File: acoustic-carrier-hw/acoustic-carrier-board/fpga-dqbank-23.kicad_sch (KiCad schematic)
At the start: 11 parts, among them IC1 ECP5-BGA256

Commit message: [carrier] finished for production (next) reroute the LPDDR3, with appropriate CMD-CTRL bus delays, and change banks for command-control
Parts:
- IC1: Manufacturer Lattice -> (none)

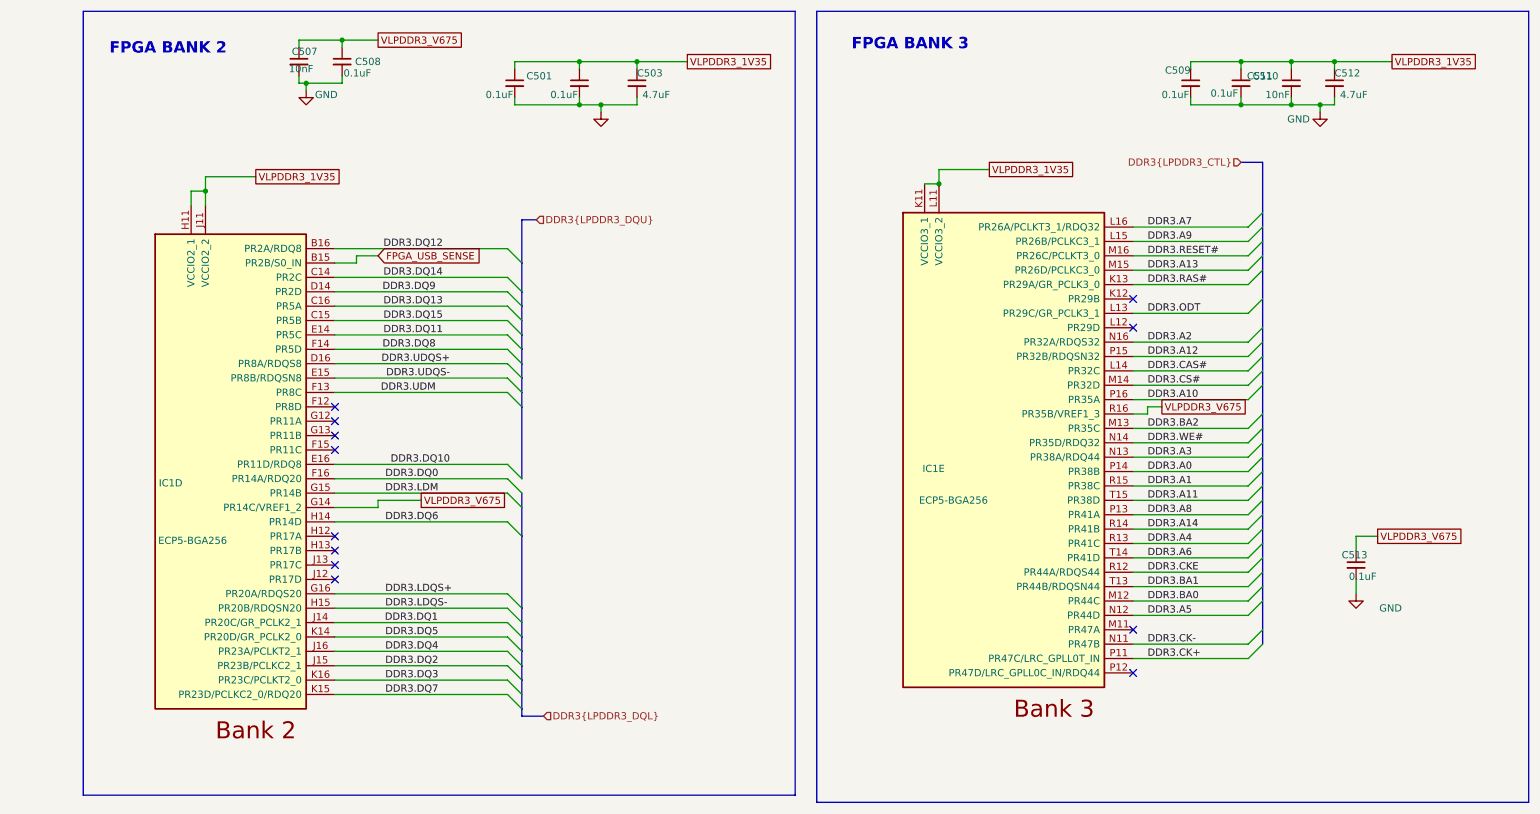
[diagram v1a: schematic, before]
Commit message: [carrier] Finished routing, layed out lpddr3 capacitors (next) route power on plane
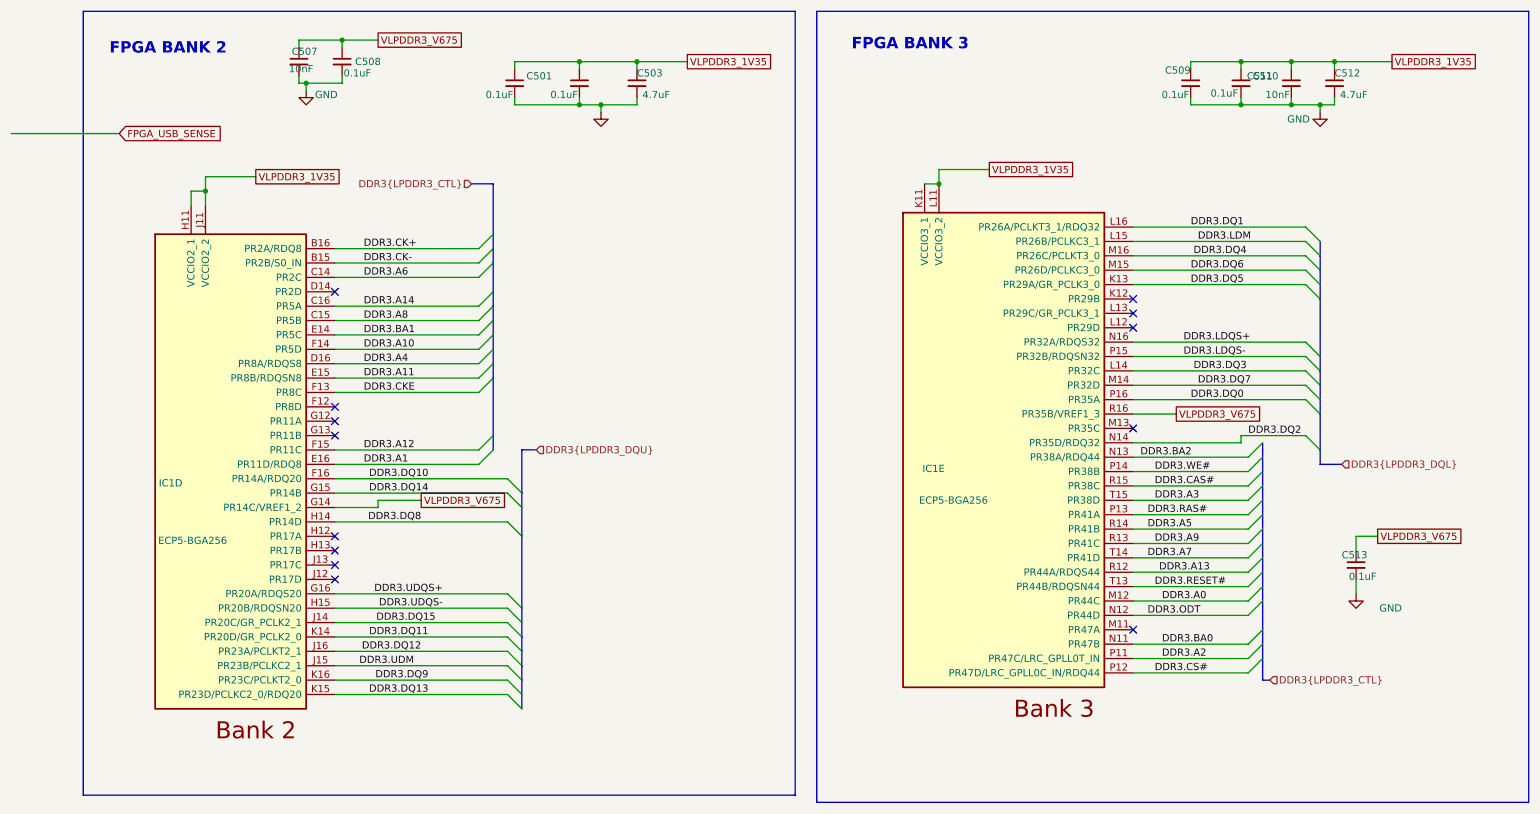
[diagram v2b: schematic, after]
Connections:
- net DDR3.A0: now also IC1.M12 (PR44C); no longer IC1.P14 (PR38B)
- net DDR3.A1: now also IC1.E16 (PR11D/RDQ8); no longer IC1.R15 (PR38C)
- net DDR3.A10: now also IC1.F14 (PR5D); no longer IC1.P16 (PR35A)
- net DDR3.A11: now also IC1.E15 (PR8B/RDQSN8); no longer IC1.T15 (PR38D)
- net DDR3.A12: now also IC1.F15 (PR11C); no longer IC1.P15 (PR32B/RDQSN32)
- net DDR3.A13: now also IC1.R12 (PR44A/RDQS44); no longer IC1.M15 (PR26D/PCLKC3_0)
- net DDR3.A14: now also IC1.C16 (PR5A); no longer IC1.R14 (PR41B)
- net DDR3.A2: now also IC1.P11 (PR47C/LRC_GPLL0T_IN); no longer IC1.N16 (PR32A/RDQS32)
- net DDR3.A3: now also IC1.T15 (PR38D); no longer IC1.N13 (PR38A/RDQ44)
- net DDR3.A4: now also IC1.D16 (PR8A/RDQS8); no longer IC1.R13 (PR41C)
- net DDR3.A5: now also IC1.R14 (PR41B); no longer IC1.N12 (PR44D)
- net DDR3.A6: now also IC1.C14 (PR2C); no longer IC1.T14 (PR41D)
- net DDR3.A7: now also IC1.T14 (PR41D); no longer IC1.L16 (PR26A/PCLKT3_1/RDQ32)
- net DDR3.A8: now also IC1.C15 (PR5B); no longer IC1.P13 (PR41A)
- net DDR3.A9: now also IC1.R13 (PR41C); no longer IC1.L15 (PR26B/PCLKC3_1)
- net DDR3.BA0: now also IC1.N11 (PR47B); no longer IC1.M12 (PR44C)
- net DDR3.BA1: now also IC1.E14 (PR5C); no longer IC1.T13 (PR44B/RDQSN44)
- net DDR3.BA2: now also IC1.N13 (PR38A/RDQ44); no longer IC1.M13 (PR35C)
- net DDR3.CAS#: now also IC1.R15 (PR38C); no longer IC1.L14 (PR32C)
- net DDR3.CK+: now also IC1.B16 (PR2A/RDQ8); no longer IC1.P11 (PR47C/LRC_GPLL0T_IN)
- net DDR3.CK-: now also IC1.B15 (PR2B/S0_IN); no longer IC1.N11 (PR47B)
- net DDR3.CKE: now also IC1.F13 (PR8C); no longer IC1.R12 (PR44A/RDQS44)
- net DDR3.CS#: now also IC1.P12 (PR47D/LRC_GPLL0C_IN/RDQ44); no longer IC1.M14 (PR32D)
- net DDR3.DQ0: now also IC1.P16 (PR35A); no longer IC1.F16 (PR14A/RDQ20)
- net DDR3.DQ1: now also IC1.L16 (PR26A/PCLKT3_1/RDQ32); no longer IC1.J14 (PR20C/GR_PCLK2_1)
- net DDR3.DQ10: now also IC1.F16 (PR14A/RDQ20); no longer IC1.E16 (PR11D/RDQ8)
- net DDR3.DQ11: now also IC1.K14 (PR20D/GR_PCLK2_0); no longer IC1.E14 (PR5C)
- net DDR3.DQ12: now also IC1.J16 (PR23A/PCLKT2_1); no longer IC1.B16 (PR2A/RDQ8)
- net DDR3.DQ13: now also IC1.K15 (PR23D/PCLKC2_0/RDQ20); no longer IC1.C16 (PR5A)
- net DDR3.DQ14: now also IC1.G15 (PR14B); no longer IC1.C14 (PR2C)
- net DDR3.DQ15: now also IC1.J14 (PR20C/GR_PCLK2_1); no longer IC1.C15 (PR5B)
- net DDR3.DQ2: now also IC1.N14 (PR35D/RDQ32); no longer IC1.J15 (PR23B/PCLKC2_1)
- net DDR3.DQ3: now also IC1.L14 (PR32C); no longer IC1.K16 (PR23C/PCLKT2_0)
- net DDR3.DQ4: now also IC1.M16 (PR26C/PCLKT3_0); no longer IC1.J16 (PR23A/PCLKT2_1)
- net DDR3.DQ5: now also IC1.K13 (PR29A/GR_PCLK3_0); no longer IC1.K14 (PR20D/GR_PCLK2_0)
- net DDR3.DQ6: now also IC1.M15 (PR26D/PCLKC3_0); no longer IC1.H14 (PR14D)
- net DDR3.DQ7: now also IC1.M14 (PR32D); no longer IC1.K15 (PR23D/PCLKC2_0/RDQ20)
- net DDR3.DQ8: now also IC1.H14 (PR14D); no longer IC1.F14 (PR5D)
- net DDR3.DQ9: now also IC1.K16 (PR23C/PCLKT2_0); no longer IC1.D14 (PR2D)
- net DDR3.LDM: now also IC1.L15 (PR26B/PCLKC3_1); no longer IC1.G15 (PR14B)
- net DDR3.LDQS+: now also IC1.N16 (PR32A/RDQS32); no longer IC1.G16 (PR20A/RDQS20)
- net DDR3.LDQS-: now also IC1.P15 (PR32B/RDQSN32); no longer IC1.H15 (PR20B/RDQSN20)
- net DDR3.ODT: now also IC1.N12 (PR44D); no longer IC1.L13 (PR29C/GR_PCLK3_1)
- net DDR3.RAS#: now also IC1.P13 (PR41A); no longer IC1.K13 (PR29A/GR_PCLK3_0)
- net DDR3.RESET#: now also IC1.T13 (PR44B/RDQSN44); no longer IC1.M16 (PR26C/PCLKT3_0)
- net DDR3.UDM: now also IC1.J15 (PR23B/PCLKC2_1); no longer IC1.F13 (PR8C)
- net DDR3.UDQS+: now also IC1.G16 (PR20A/RDQS20); no longer IC1.D16 (PR8A/RDQS8)
- net DDR3.UDQS-: now also IC1.H15 (PR20B/RDQSN20); no longer IC1.E15 (PR8B/RDQSN8)
- net DDR3.WE#: now also IC1.P14 (PR38B); no longer IC1.N14 (PR35D/RDQ32)
- net FPGA_USB_SENSE: no longer IC1.B15 (PR2B/S0_IN)
- no-connect marks 12 -> 13

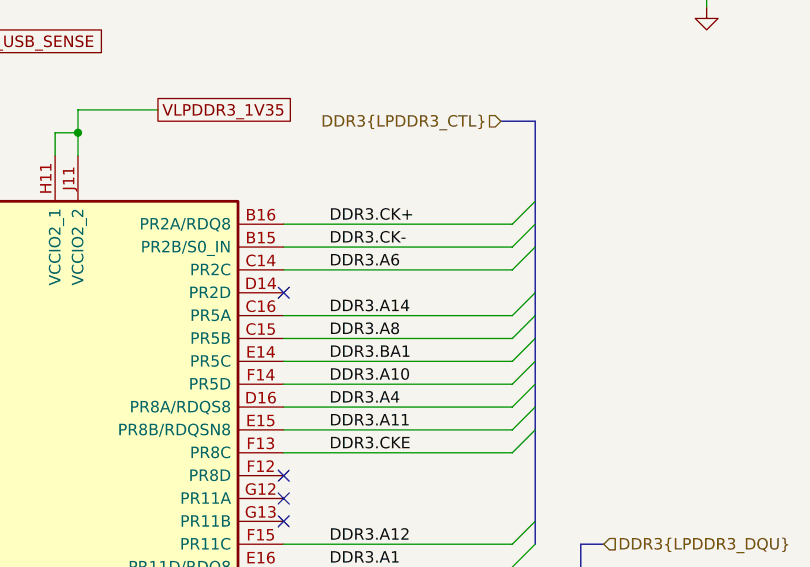
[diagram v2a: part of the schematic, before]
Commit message: [carrier] Added testpoints (next) schematic review, (optional) simulation, submit to jlc
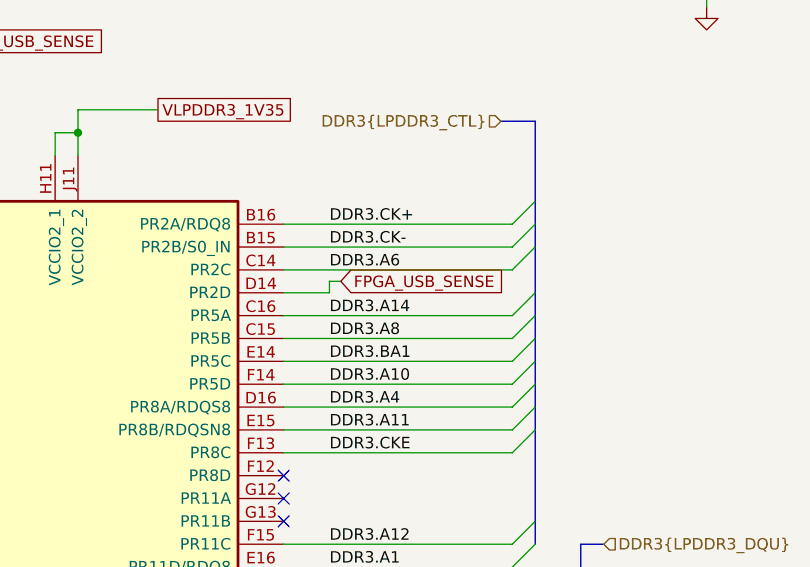
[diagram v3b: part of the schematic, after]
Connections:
- net FPGA_USB_SENSE: now also IC1.D14 (PR2D)
- no-connect marks 13 -> 12
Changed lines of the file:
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@@
-	)
-	(no_connect
-		(at 71.12 69.85)
 	)
 	(no_connect
@@
 	(wire
 		(pts
+			(xy 76.2 69.85) (xy 71.12 69.85)
+		)
+		(stroke
+			(width 0)
+			(type default)
+		)
+	)
+	(wire
+		(pts
 			(xy 231.14 36.83) (xy 240.03 36.83)
 		)
@@
 	(wire
 		(pts
+			(xy 76.2 68.58) (xy 76.2 69.85)
+		)
+		(stroke
+			(width 0)
+			(type default)
+		)
+	)
+	(wire
+		(pts
 			(xy 231.14 95.25) (xy 231.14 96.52)
 		)
@@
 		(pts
 			(xy 71.12 110.49) (xy 101.6 110.49)
+		)
+		(stroke
+			(width 0)
+			(type default)
+		)
+	)
+	(wire
+		(pts
+			(xy 76.2 68.58) (xy 77.47 68.58)
 		)
 		(stroke
@@
 			(effects
 				(font
+					(size 1.27 1.27)
+				)
+				(justify left)
+				(hide yes)
+			)
+		)
+	)
+	(global_label "FPGA_USB_SENSE"
+		(shape input)
+		(at 77.47 68.58 0)
+		(fields_autoplaced yes)
+		(effects
+			(font
+				(size 1.27 1.27)
+			)
+			(justify left)
+		)
+		(property "Intersheetrefs" "${INTERSHEET_REFS}"
+			(at 96.9651 68.58 0)
+			(effects
+				(font

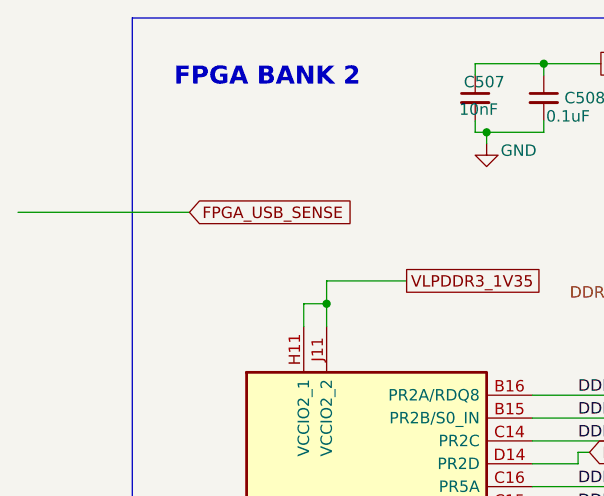
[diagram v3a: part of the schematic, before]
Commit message: [carrier] Added more return vias (next) move to separate repo
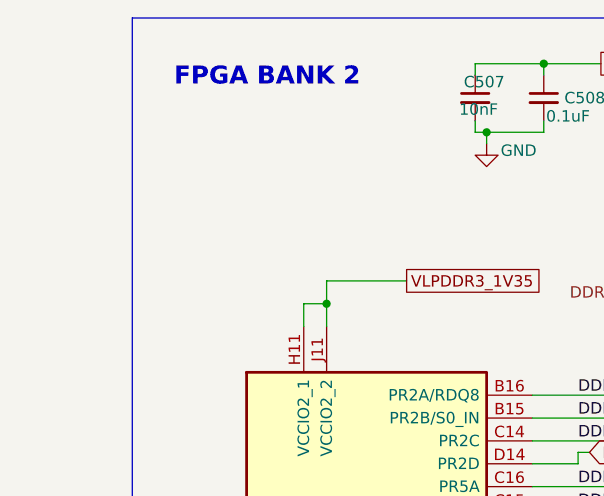
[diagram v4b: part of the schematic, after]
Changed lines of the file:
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@@
-	(wire
-		(pts
-			(xy 13.97 41.91) (xy 33.02 41.91)
-		)
-		(stroke
-			(width 0)
-			(type default)
-		)
-	)
 	(wire
 		(pts
@@
 			(effects
 				(font
-					(size 1.27 1.27)
-				)
-				(justify left)
-				(hide yes)
-			)
-		)
-	)
-	(global_label "FPGA_USB_SENSE"
-		(shape input)
-		(at 33.02 41.91 0)
-		(fields_autoplaced yes)
-		(effects
-			(font
-				(size 1.27 1.27)
-			)
-			(justify left)
-		)
-		(property "Intersheetrefs" "${INTERSHEET_REFS}"
-			(at 52.5151 41.91 0)
-			(effects
-				(font
